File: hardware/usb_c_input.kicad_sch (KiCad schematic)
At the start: 3 parts, among them J7 USB_C_Receptacle_USB2.0_16P, U10 TPD4EUSB30

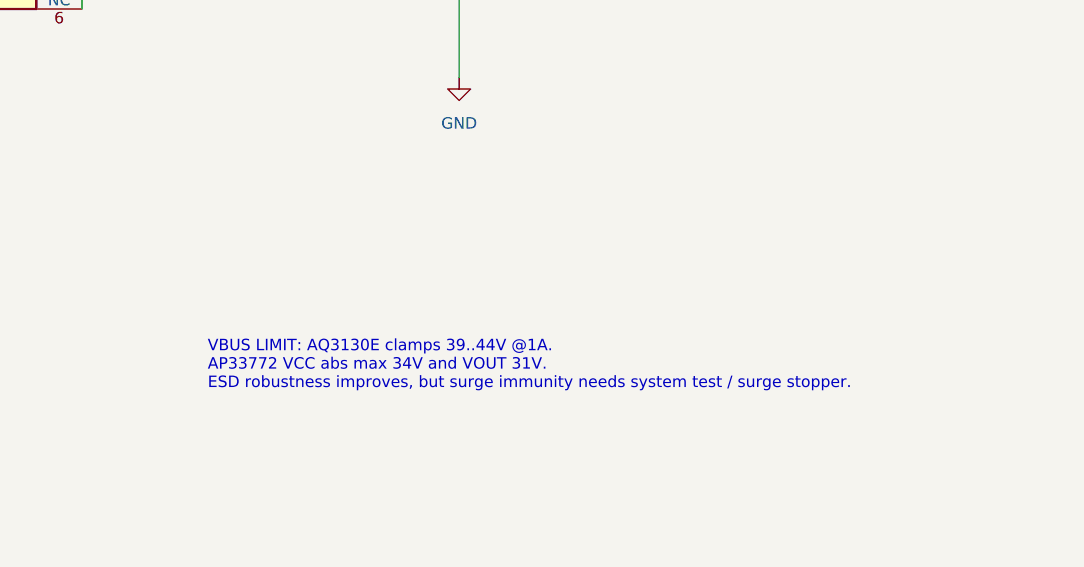
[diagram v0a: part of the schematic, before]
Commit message: usb_c_input: notu başlık bloğunun üstünden taşı, D3 bilgisini güncelle
Not AQ3130E'den söz ediyordu; D3 SMBJ30A. Netlist değişmedi.

Co-Authored-By: Claude Opus 5 <noreply@anthropic.com>
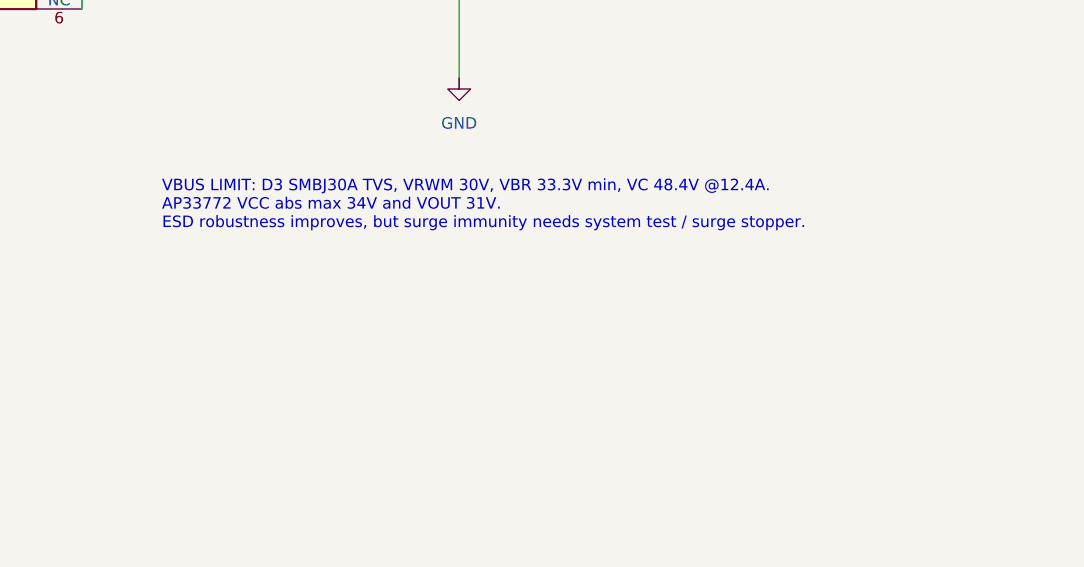
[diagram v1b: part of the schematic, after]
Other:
- note added: "VBUS LIMIT: D3 SMBJ30A TVS, VRWM 30V, VBR 33.3V min, VC 48.4V @12.4A. AP33772 VCC abs max 34V and VOUT 31V. ESD robustness improves, but surge immunity needs system test / surge stopper."
- note removed: "VBUS LIMIT: AQ3130E clamps 39..44V @1A. AP33772 VCC abs max 34V and VOUT 31V. ESD robustness improves, but surge immunity needs system test / surge stopper."
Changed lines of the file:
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@@
 	(generator_version "10.0")
 	(paper "A4")
-	(text "VBUS LIMIT: AQ3130E clamps 39..44V @1A.\nAP33772 VCC abs max 34V and VOUT 31V.\nESD robustness improves, but surge immunity needs system test / surge stopper."
+	(text "VBUS LIMIT: D3 SMBJ30A TVS, VRWM 30V, VBR 33.3V min, VC 48.4V @12.4A.\nAP33772 VCC abs max 34V and VOUT 31V.\nESD robustness improves, but surge immunity needs system test / surge stopper."
 		(exclude_from_sim no)
-		(at 182.88 160.02 0)
+		(at 177.8 142.24 0)
 		(effects
 			(font
